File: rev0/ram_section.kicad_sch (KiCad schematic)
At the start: 2 parts, among them IC1 ECP5-BGA256, U10 HyperRAM

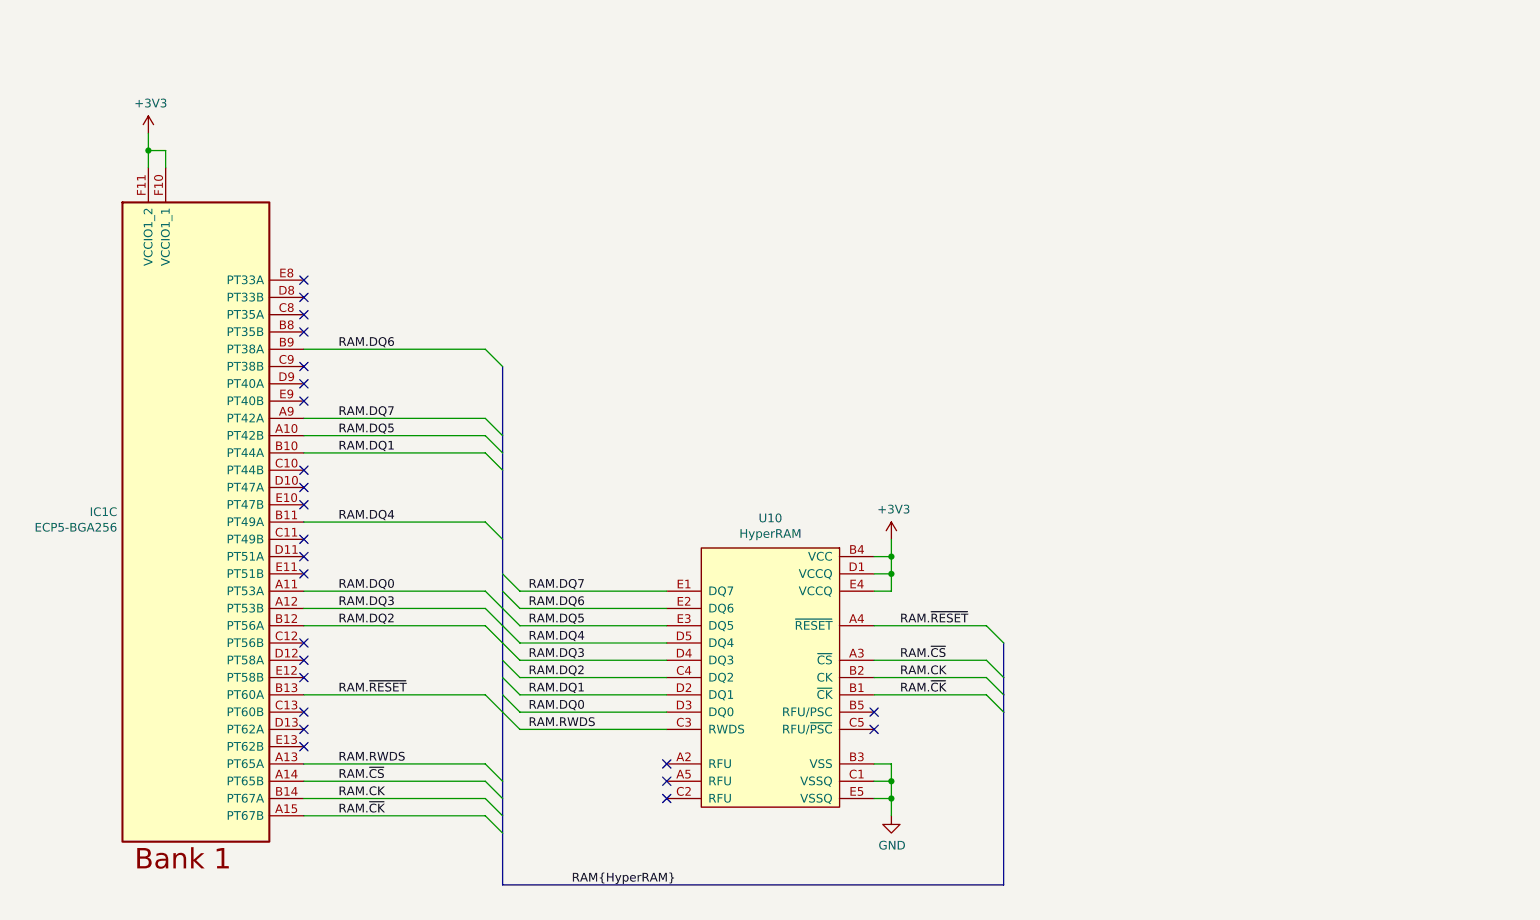
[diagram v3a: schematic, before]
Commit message: hardware: restore 1.8 V RAM supply as an option
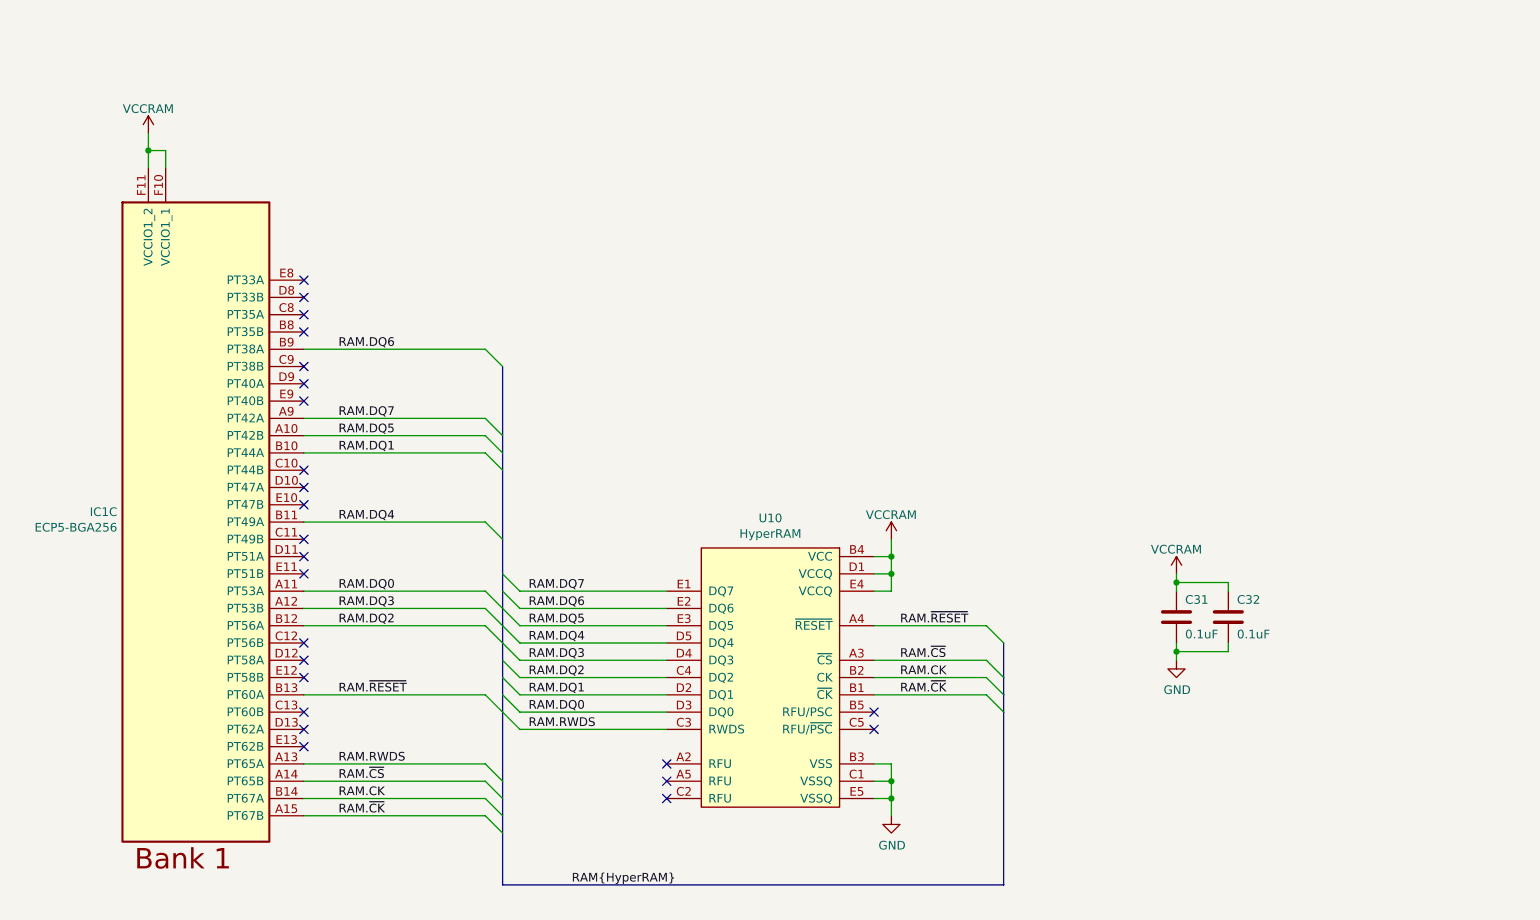
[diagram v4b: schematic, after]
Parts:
- added C31, C32: 0.1uF, Capacitor_SMD:C_0402_1005Metric, symbol Device:C
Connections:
- net GND: now also C31.2, C32.2
- net +3V3 renamed VCCRAM
- net VCCRAM: now also C31.1, C32.1
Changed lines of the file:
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@@
   )
   (bus_alias "HyperRAM" (members "DQ[0..7]" "CK" "~{CK}" "~{CS}" "RWDS" "~{RESET}"))
+  (junction (at 196.85 109.22) (diameter 0) (color 0 0 0 0)
+  )
   (junction (at 154.94 138.43) (diameter 0) (color 0 0 0 0)
   )
@@
   )
   (junction (at 154.94 107.95) (diameter 0) (color 0 0 0 0)
+  )
+  (junction (at 196.85 119.38) (diameter 0) (color 0 0 0 0)
   )
   (no_connect (at 68.58 123.19))
@@
     (stroke (width 0) (type default) (color 0 0 0 0))
   )
+  (wire (pts (xy 196.85 107.95) (xy 196.85 109.22))
+    (stroke (width 0) (type default) (color 0 0 0 0))
+  )
+  (wire (pts (xy 196.85 119.38) (xy 196.85 120.65))
+    (stroke (width 0) (type default) (color 0 0 0 0))
+  )
   (wire (pts (xy 152.4 115.57) (xy 168.91 115.57))
     (stroke (width 0) (type default) (color 0 0 0 0))
@@
     (stroke (width 0) (type default) (color 0 0 0 0))
   )
+  (wire (pts (xy 204.47 109.22) (xy 204.47 110.49))
+    (stroke (width 0) (type default) (color 0 0 0 0))
+  )
   (wire (pts (xy 68.58 90.17) (xy 95.25 90.17))
     (stroke (width 0) (type default) (color 0 0 0 0))
@@
     (stroke (width 0) (type default) (color 0 0 0 0))
   )
+  (wire (pts (xy 196.85 109.22) (xy 196.85 110.49))
+    (stroke (width 0) (type default) (color 0 0 0 0))
+  )
   (bus (pts (xy 97.79 107.95) (xy 97.79 110.49))
     (stroke (width 0) (type default) (color 0 0 0 0))
@@
     (stroke (width 0) (type default) (color 0 0 0 0))
   )
+  (wire (pts (xy 196.85 109.22) (xy 204.47 109.22))
+    (stroke (width 0) (type default) (color 0 0 0 0))
+  )
   (bus (pts (xy 97.79 123.19) (xy 97.79 125.73))
     (stroke (width 0) (type default) (color 0 0 0 0))
@@
     (stroke (width 0) (type default) (color 0 0 0 0))
   )
+  (wire (pts (xy 196.85 119.38) (xy 204.47 119.38))
+    (stroke (width 0) (type default) (color 0 0 0 0))
+  )
   (wire (pts (xy 154.94 105.41) (xy 154.94 102.87))
     (stroke (width 0) (type default) (color 0 0 0 0))
@@
     (stroke (width 0) (type default) (color 0 0 0 0))
   )
+  (wire (pts (xy 204.47 119.38) (xy 204.47 118.11))
+    (stroke (width 0) (type default) (color 0 0 0 0))
+  )
   (wire (pts (xy 154.94 140.97) (xy 152.4 140.97))
     (stroke (width 0) (type default) (color 0 0 0 0))
@@
   )
   (bus (pts (xy 97.79 143.51) (xy 97.79 146.05))
+    (stroke (width 0) (type default) (color 0 0 0 0))
+  )
+  (wire (pts (xy 196.85 118.11) (xy 196.85 119.38))
     (stroke (width 0) (type default) (color 0 0 0 0))
   )
@@
     (pin "1")
   )
-  (symbol (lib_id "power:+3V3") (at 45.72 43.18 0) (unit 1)
+  (symbol (lib_id "power:GND") (at 196.85 120.65 0) (unit 1)
     (in_bom yes) (on_board yes)
-    (property "Reference" "#PWR0118" (id 0) (at 45.72 46.99 0)
-      (effects (font (size 1.27 1.27)) hide)
-    )
-    (property "Value" "+3V3" (id 1) (at 46.0756 38.7858 0))
+    (property "Reference" "#PWR?" (id 0) (at 196.85 127 0)
+      (effects (font (size 1.27 1.27)) hide)
+    )
+    (property "Value" "GND" (id 1) (at 196.9516 125.0188 0))
+    (property "Footprint" "" (id 2) (at 196.85 120.65 0)
+      (effects (font (size 1.27 1.27)) hide)
+    )
+    (property "Datasheet" "" (id 3) (at 196.85 120.65 0)
+      (effects (font (size 1.27 1.27)) hide)
+    )
+    (pin "1")
+  )
+  (symbol (lib_id "support_hardware:VCCRAM") (at 45.72 43.18 0) (unit 1)
+    (in_bom yes) (on_board yes) (fields_autoplaced)
+    (property "Reference" "#PWR?" (id 0) (at 45.72 46.99 0)
+      (effects (font (size 1.27 1.27)) hide)
+    )
+    (property "Value" "VCCRAM" (id 1) (at 45.72 39.6042 0))
     (property "Footprint" "" (id 2) (at 45.72 43.18 0)
       (effects (font (size 1.27 1.27)) hide)
@@
     (pin "1")
   )
-  (symbol (lib_id "power:+3V3") (at 154.94 102.87 0) (unit 1)
+  (symbol (lib_id "support_hardware:VCCRAM") (at 154.94 102.87 0) (unit 1)
+    (in_bom yes) (on_board yes) (fields_autoplaced)
+    (property "Reference" "#PWR?" (id 0) (at 154.94 106.68 0)
+      (effects (font (size 1.27 1.27)) hide)
+    )
+    (property "Value" "VCCRAM" (id 1) (at 154.94 99.2942 0))
+    (property "Footprint" "" (id 2) (at 154.94 102.87 0)
+      (effects (font (size 1.27 1.27)) hide)
+    )
+    (property "Datasheet" "" (id 3) (at 154.94 102.87 0)
+      (effects (font (size 1.27 1.27)) hide)
+    )
+    (pin "1")
+  )
+  (symbol (lib_id "Device:C") (at 196.85 114.3 0) (unit 1)
     (in_bom yes) (on_board yes)
-    (property "Reference" "#PWR0119" (id 0) (at 154.94 106.68 0)
-      (effects (font (size 1.27 1.27)) hide)
-    )
-    (property "Value" "+3V3" (id 1) (at 155.2956 98.4758 0))
-    (property "Footprint" "" (id 2) (at 154.94 102.87 0)
-      (effects (font (size 1.27 1.27)) hide)
-    )
-    (property "Datasheet" "" (id 3) (at 154.94 102.87 0)
-      (effects (font (size 1.27 1.27)) hide)
-    )
+    (property "Reference" "C31" (id 0) (at 198.12 111.76 0)
+      (effects (font (size 1.27 1.27)) (justify left))
+    )
+    (property "Value" "0.1uF" (id 1) (at 198.12 116.84 0)
+      (effects (font (size 1.27 1.27)) (justify left))
+    )
+    (property "Footprint" "Capacitor_SMD:C_0402_1005Metric" (id 2) (at 197.8152 118.11 0)
+      (effects (font (size 1.27 1.27)) hide)
+    )
+    (property "Datasheet" "~" (id 3) (at 196.85 114.3 0)
+      (effects (font (size 1.27 1.27)) hide)
+    )
+    (property "Part Number" "GENERIC-CAP-0402-0.1uF" (id 4) (at 196.85 114.3 0)
+      (effects (font (size 1.27 1.27)) hide)
+    )
+    (property "Substitution" "any equivalent" (id 5) (at 196.85 114.3 0)
+      (effects (font (size 1.27 1.27)) hide)
+    )
+    (pin "1")
+    (pin "2")
+  )
+  (symbol (lib_id "Device:C") (at 204.47 114.3 0) (unit 1)
+    (in_bom yes) (on_board yes)
+    (property "Reference" "C32" (id 0) (at 205.74 111.76 0)
+      (effects (font (size 1.27 1.27)) (justify left))
+    )
+    (property "Value" "0.1uF" (id 1) (at 205.74 116.84 0)
+      (effects (font (size 1.27 1.27)) (justify left))
+    )
+    (property "Footprint" "Capacitor_SMD:C_0402_1005Metric" (id 2) (at 205.4352 118.11 0)
+      (effects (font (size 1.27 1.27)) hide)
+    )
+    (property "Datasheet" "~" (id 3) (at 204.47 114.3 0)
+      (effects (font (size 1.27 1.27)) hide)
+    )
+    (property "Part Number" "GENERIC-CAP-0402-0.1uF" (id 4) (at 204.47 114.3 0)
+      (effects (font (size 1.27 1.27)) hide)
+    )
+    (property "Substitution" "any equivalent" (id 5) (at 204.47 114.3 0)
+      (effects (font (size 1.27 1.27)) hide)
+    )
+    (pin "1")
+    (pin "2")
+  )
+  (symbol (lib_id "support_hardware:VCCRAM") (at 196.85 107.95 0) (unit 1)
+    (in_bom yes) (on_board yes) (fields_autoplaced)
+    (property "Reference" "#PWR?" (id 0) (at 196.85 111.76 0)
+      (effects (font (size 1.27 1.27)) hide)
+    )
+    (property "Value" "VCCRAM" (id 1) (at 196.85 104.3742 0))
+    (property "Footprint" "" (id 2) (at 196.85 107.95 0)
+      (effects (font (size 1.27 1.27)) hide)
+    )
+    (property "Datasheet" "" (id 3) (at 196.85 107.95 0)
+      (effects (font (size 1.27 1.27)) hide)
+    )

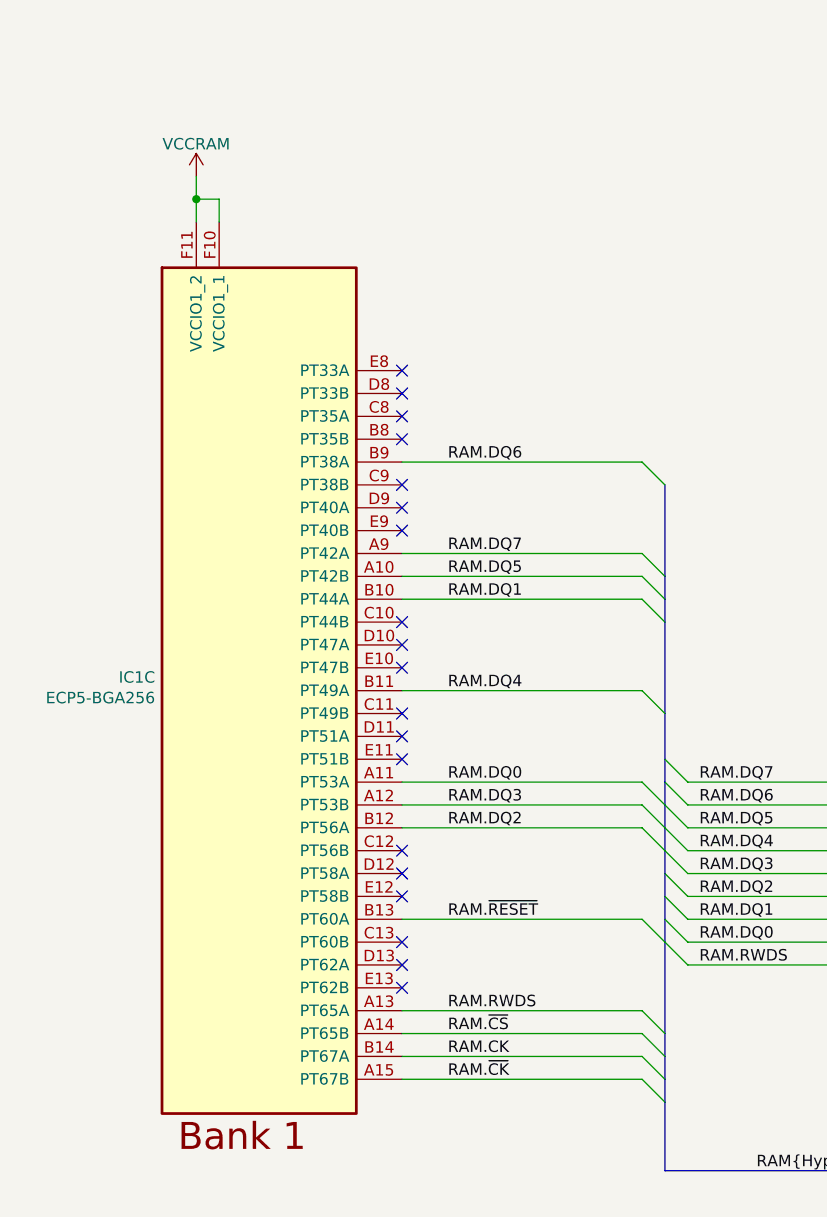
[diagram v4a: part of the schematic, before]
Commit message: hardware: reassign FPGA I/O banks
assign HyperRAM to DQS group
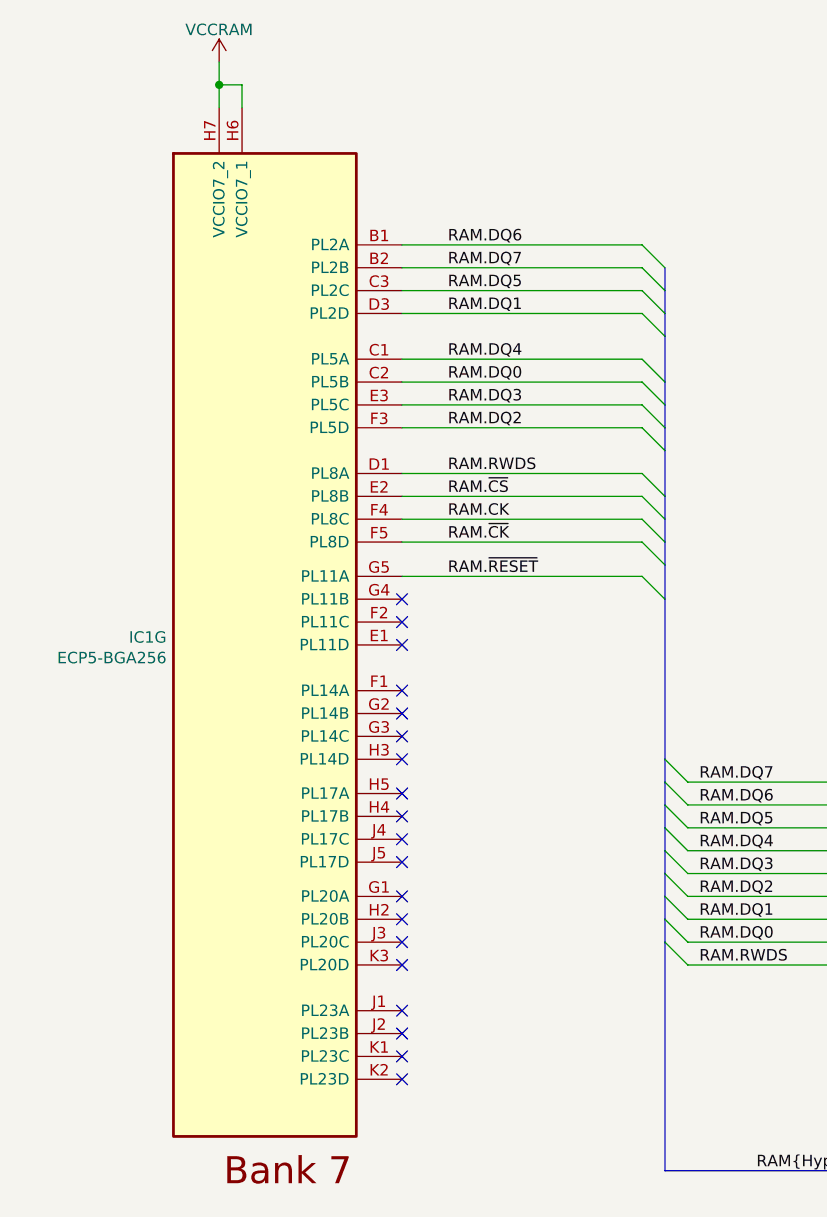
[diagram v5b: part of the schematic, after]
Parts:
- removed IC1: ECP5-BGA256, luna:lattice_cabga256, symbol fpgas_and_processors:ECP5-BGA256
- added IC1: ECP5-BGA256, luna:lattice_cabga256, symbol fpgas_and_processors:ECP5-BGA256
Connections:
- net RAM.CK: now also IC1.F4 (PL8C)
- net RAM.DQ0: now also IC1.C2 (PL5B)
- net RAM.DQ1: now also IC1.D3 (PL2D)
- net RAM.DQ2: now also IC1.F3 (PL5D)
- net RAM.DQ3: now also IC1.E3 (PL5C)
- net RAM.DQ4: now also IC1.C1 (PL5A)
- net RAM.DQ5: now also IC1.C3 (PL2C)
- net RAM.DQ6: now also IC1.B1 (PL2A)
- net RAM.DQ7: now also IC1.B2 (PL2B)
- net RAM.RWDS: now also IC1.D1 (PL8A)
- net RAM.~{CK}: now also IC1.F5 (PL8D)
- net RAM.~{CS}: now also IC1.E2 (PL8B)
- net RAM.~{RESET}: now also IC1.G5 (PL11A)
- net VCCRAM: now also IC1.H6 (VCCIO7_1), IC1.H7 (VCCIO7_2)
